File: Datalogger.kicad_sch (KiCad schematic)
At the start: 0 parts

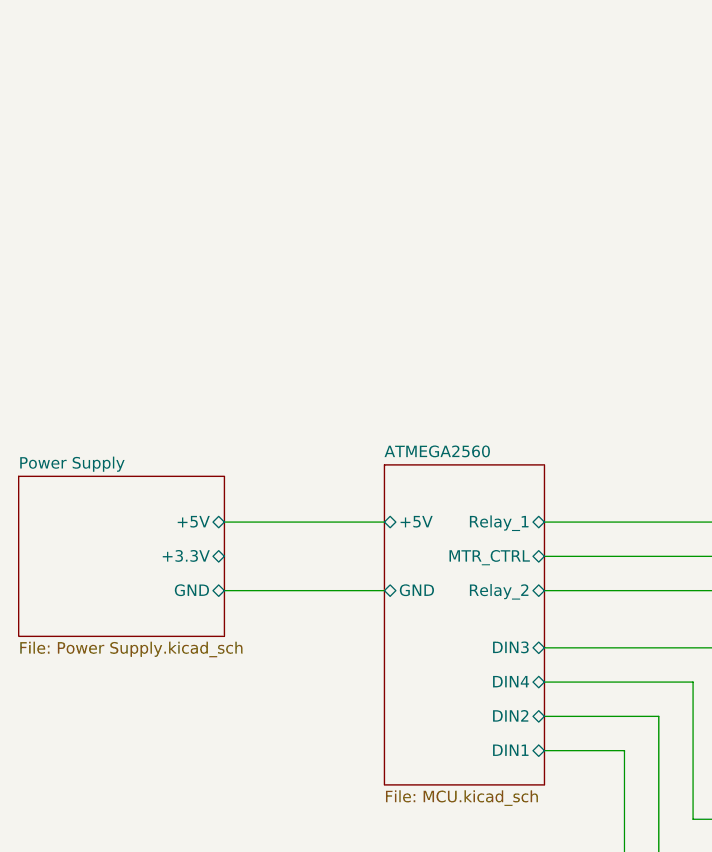
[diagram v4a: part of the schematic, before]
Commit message: Schematic of 4-20mA sensor
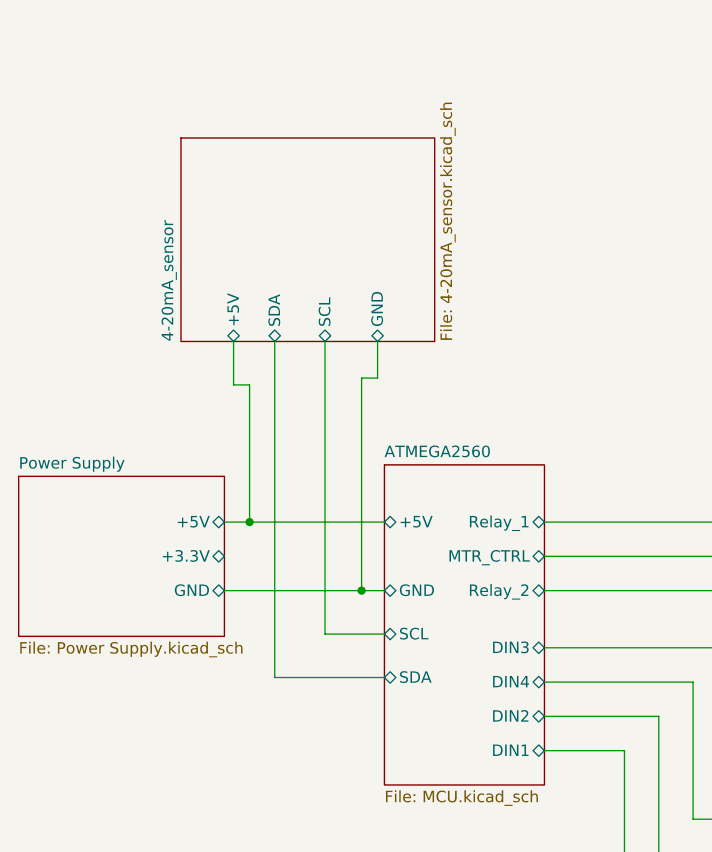
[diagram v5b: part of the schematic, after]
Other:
- added sheet 4-20mA_sensor (4-20mA_sensor.kicad_sch)
- sheet ATMEGA2560 ports: added SCL, SDA; removed none
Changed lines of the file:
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@@
 (kicad_sch (version 20230121) (generator eeschema)
   (paper "A4")
+  (junction (at 113.284 93.98) (diameter 0) (color 0 0 0 0)
+  )
+  (junction (at 125.73 101.6) (diameter 0) (color 0 0 0 0)
+  )
   (wire (pts (xy 154.94 134.62) (xy 170.18 134.62))
     (stroke (width 0) (type default))
@@
     (stroke (width 0) (type default))
   )
+  (wire (pts (xy 127.508 77.978) (xy 125.73 77.978))
+    (stroke (width 0) (type default))
+  )
   (wire (pts (xy 146.05 101.6) (xy 170.18 101.6))
     (stroke (width 0) (type default))
   )
-  (wire (pts (xy 110.49 101.6) (xy 128.27 101.6))
+  (wire (pts (xy 110.49 101.6) (xy 125.73 101.6))
     (stroke (width 0) (type default))
   )
@@
     (stroke (width 0) (type default))
   )
+  (wire (pts (xy 111.506 78.74) (xy 113.284 78.74))
+    (stroke (width 0) (type default))
+  )
+  (wire (pts (xy 113.284 78.74) (xy 113.284 93.98))
+    (stroke (width 0) (type default))
+  )
+  (wire (pts (xy 127.508 73.914) (xy 127.508 77.978))
+    (stroke (width 0) (type default))
+  )
   (wire (pts (xy 146.05 93.98) (xy 170.18 93.98))
     (stroke (width 0) (type default))
@@
     (stroke (width 0) (type default))
   )
-  (wire (pts (xy 110.49 93.98) (xy 128.27 93.98))
+  (wire (pts (xy 110.49 93.98) (xy 113.284 93.98))
     (stroke (width 0) (type default))
   )
@@
     (stroke (width 0) (type default))
   )
+  (wire (pts (xy 116.078 111.252) (xy 128.27 111.252))
+    (stroke (width 0) (type default))
+  )
   (wire (pts (xy 166.37 107.95) (xy 166.37 123.19))
     (stroke (width 0) (type default))
@@
     (stroke (width 0) (type default))
   )
+  (wire (pts (xy 113.284 93.98) (xy 128.27 93.98))
+    (stroke (width 0) (type default))
+  )
+  (wire (pts (xy 128.27 106.426) (xy 121.666 106.426))
+    (stroke (width 0) (type default))
+  )
   (wire (pts (xy 162.56 127) (xy 170.18 127))
     (stroke (width 0) (type default))
   )
+  (wire (pts (xy 116.078 73.914) (xy 116.078 111.252))
+    (stroke (width 0) (type default))
+  )
+  (wire (pts (xy 125.73 101.6) (xy 128.27 101.6))
+    (stroke (width 0) (type default))
+  )
   (wire (pts (xy 146.05 97.79) (xy 170.18 97.79))
     (stroke (width 0) (type default))
   )
+  (wire (pts (xy 125.73 77.978) (xy 125.73 101.6))
+    (stroke (width 0) (type default))
+  )
   (wire (pts (xy 158.75 115.57) (xy 158.75 130.81))
     (stroke (width 0) (type default))
@@
     (stroke (width 0) (type default))
   )
+  (wire (pts (xy 121.666 106.426) (xy 121.666 73.914))
+    (stroke (width 0) (type default))
+  )
+  (wire (pts (xy 111.506 73.914) (xy 111.506 78.74))
+    (stroke (width 0) (type default))
+  )
   (wire (pts (xy 162.56 111.76) (xy 162.56 127))
     (stroke (width 0) (type default))
@@
       (project "Datalogger"
         (path "/9962467c-5981-4f6d-a8e0-b5534b13e1af" (page "2"))
+      )
+    )
+  )
+  (sheet (at 105.664 51.308) (size 28.194 22.606) (fields_autoplaced)
+    (stroke (width 0.1524) (type solid))
+    (fill (color 0 0 0 0.0000))
+    (property "Sheetname" "4-20mA_sensor" (at 104.9524 73.914 90)
+      (effects (font (size 1.27 1.27)) (justify left bottom))
+    )
+    (property "Sheetfile" "4-20mA_sensor.kicad_sch" (at 134.4426 73.914 90)
+      (effects (font (size 1.27 1.27)) (justify left top))
+    )
+    (pin "+5V" bidirectional (at 111.506 73.914 270)
+      (effects (font (size 1.27 1.27)) (justify left))
+    )
+    (pin "SDA" bidirectional (at 116.078 73.914 270)
+      (effects (font (size 1.27 1.27)) (justify left))
+    )
+    (pin "SCL" bidirectional (at 121.666 73.914 270)
+      (effects (font (size 1.27 1.27)) (justify left))
+    )
+    (pin "GND" bidirectional (at 127.508 73.914 270)
+      (effects (font (size 1.27 1.27)) (justify left))
+    )
+    (instances
+      (project "Datalogger"
+        (path "/9962467c-5981-4f6d-a8e0-b5534b13e1af" (page "6"))
       )
     )
@@
       (effects (font (size 1.27 1.27)) (justify right))
     )
-    (instances
+    (pin "SCL" bidirectional (at 128.27 106.426 180)
+      (effects (font (size 1.27 1.27)) (justify left))
+    )
+    (pin "SDA" bidirectional (at 128.27 111.252 180)
+      (effects (font (size 1.27 1.27)) (justify left))
+    )
+    (instances
